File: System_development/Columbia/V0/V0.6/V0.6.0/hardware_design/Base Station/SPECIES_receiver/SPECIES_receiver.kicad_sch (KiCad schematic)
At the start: 8 parts, among them J1 Conn_02x04_Odd_Even_MountingP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, J2 Conn_02x04_Odd_Even_MountingP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, J3 Conn_02x20_Odd_Even

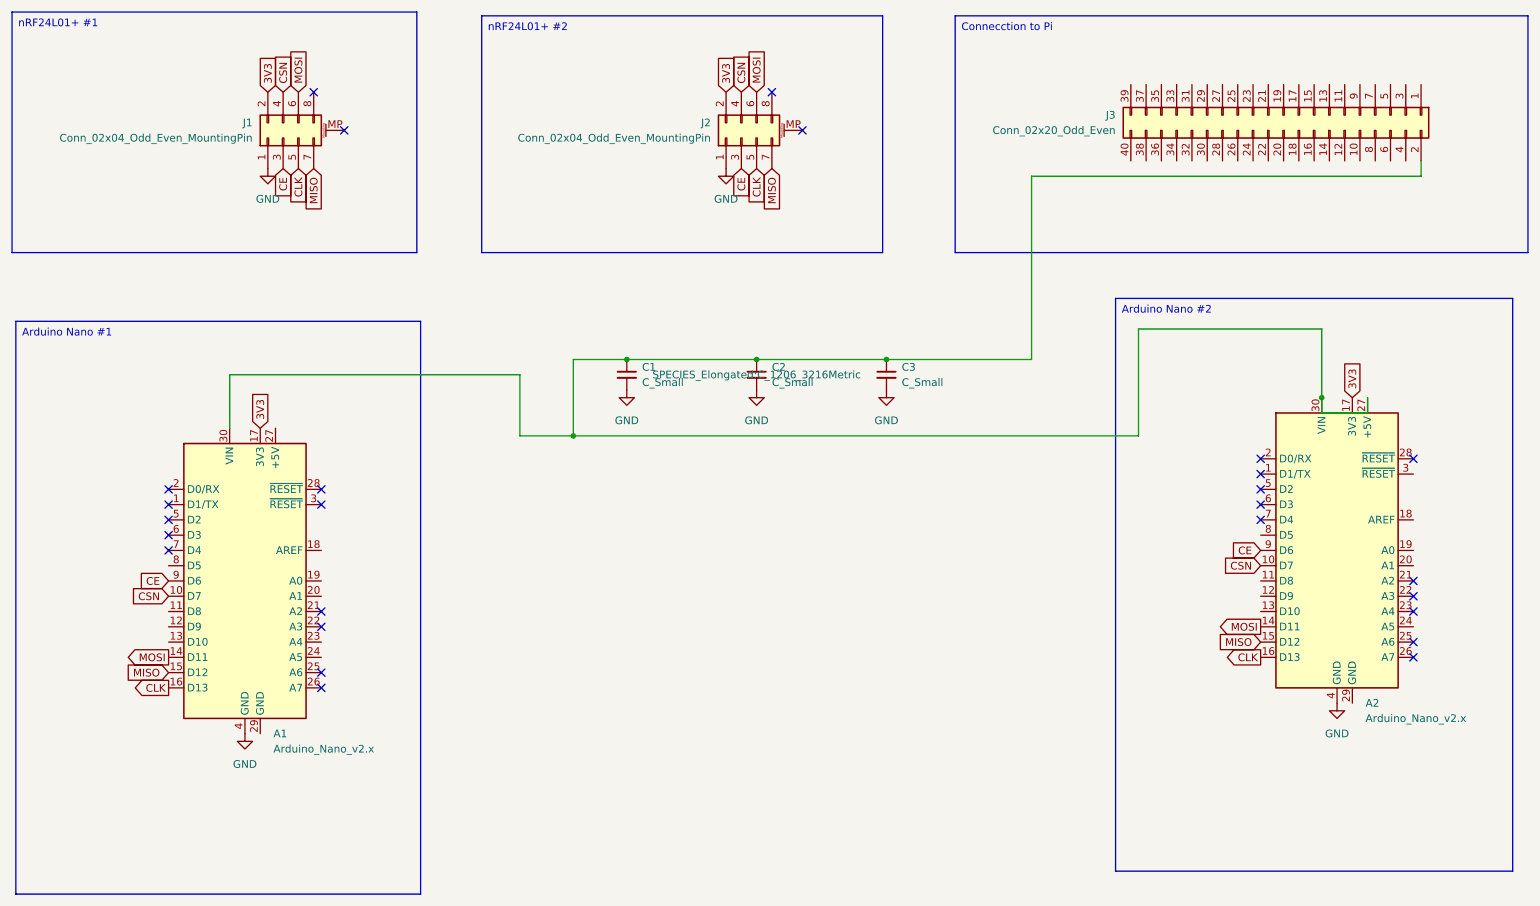
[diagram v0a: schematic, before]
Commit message: updated base station receiver pcb
decreased board size, flipped nRF pinout, and added clearer silkscreen labels
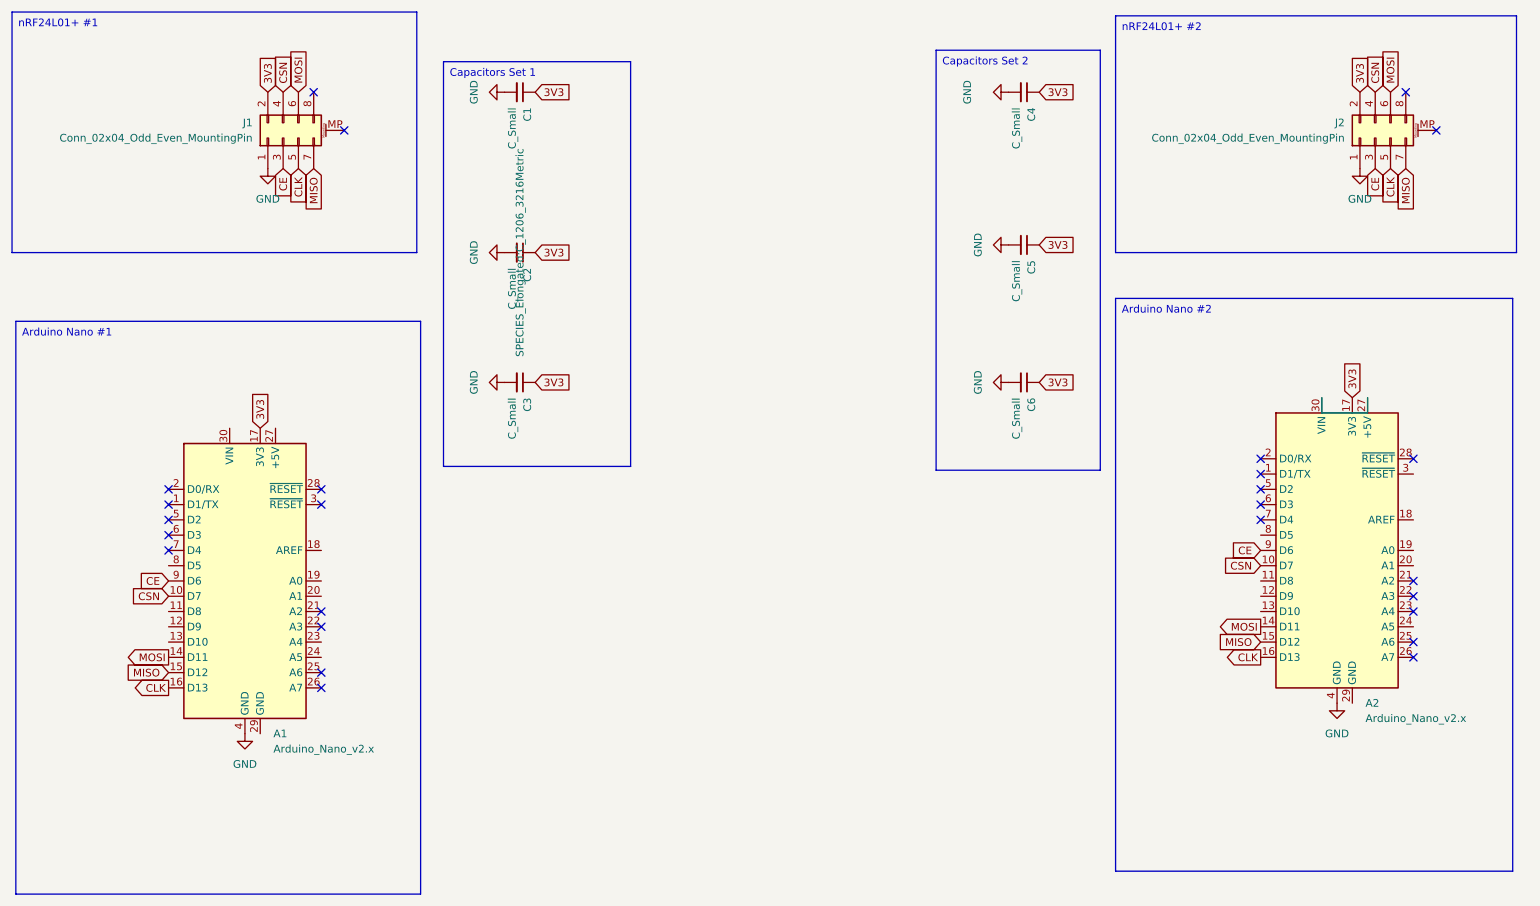
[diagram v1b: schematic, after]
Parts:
- removed J3: Conn_02x20_Odd_Even, Connector_PinSocket_2.54mm:PinSocket_2x20_P2.54mm_Vertical, symbol Connector_Generic:Conn_02x20_Odd_Even
- added C4, C5, C6: C_Small, SPECIES_Elongated:C_1206_3216Metric, symbol Device:C_Small
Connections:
- net 3V3: now also C1.1, C2.1, C3.1, C4.1, C5.1, C6.1
- net GND: now also C4.2, C5.2, C6.2
- new net: A2.27 (+5V), A2.30 (VIN)
- now unconnected: A1.30 (VIN)
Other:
- company: (none) -> Sydney Morris - ARTS Lab
- title: (none) -> Receiver PCB for Base Station
- moved on the sheet: C1, C2, C3, J2
